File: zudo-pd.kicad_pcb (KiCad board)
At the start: 2 copper layers, 82 x 99 mm, 81 parts, among them J1 USB-C, J2 2541WR-2X08P, J3 2541WR-2X08P, J4 2541WR-2X08P, J6 1217754-1, J7 1217754-1, J8 1217754-1, J9 1217754-1, U1 CH224D, U2 LM2596S-ADJ, U3 LM2596S-ADJ, U4 LM2596S-ADJ, U6 L7812CD2T-TR, U7 L7805ABD2T-TR, U8 CJ7912_C94173

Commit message: feat: Add USBLC6-2SC6 footprint and sync schematic to PCB
- Add SOT-23-6 footprint for D4 (USBLC6-2SC6) to library
- Sync all schematic changes to PCB layout

Co-Authored-By: Claude <noreply@anthropic.com>
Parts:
- removed ?: , 
- removed J3, J4: 2541WR-2X08P, zudo-pd:HDR-TH_16P-P2.54-H-M-R2-C8-S2.54
- removed REF** (x6): MountingHole_3.2mm_M3, MountingHole:MountingHole_3.2mm_M3
- added C34: 1uF 16V, zudo-pd:C0603, F.Cu at (81.8, -22.6)
- added C35: 100nF 50V, zudo-pd:C0805, F.Cu at (83.7, -30.8)
- added D4: USBLC6-2SC6, zudo-pd:SOT-23-6_L2.9-W1.6-P0.95-LS2.8-BL, F.Cu at (65.8, -22.2)
- added Q1: -30V -4A, zudo-pd:SOT-23_L2.9-W1.3-P1.90-LS2.4-BR, F.Cu at (64.5, -8.35)
- C30: value 1uF -> 1uF 16V
- R11: value 56k -> 100k
- R12: value 5.1k -> 56k
- R13: value 5.1k -> 470
- U1: value CH224D -> STUSB4500QTR; footprint zudo-pd:QFN-20_L3.0-W3.0-P0.40-BL-EP1.7 -> zudo-pd:QFN-24_L4.0-W4.0-P0.50-BL-EP2.8
- moved R12 59.7 mm to (85.7, -22.9)
- moved R13 57.3 mm to (85.7, -20.4), turned to 0 degrees
- moved C30 55.4 mm to (81.8, -25.3), turned to 0 degrees
- moved R11 50.5 mm to (85.7, -25.4)
- moved U1 8.08 mm to (43.5, 6.00), turned to 90 degrees
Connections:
- C1 pad 2: +15V -> +13.5V gen -> VBUS_IN
- C2 pad 2: +15V -> +13.5V gen -> VBUS_IN
- C30 pad 1: Net-(U1-VDD) -> Net-(U1-VREG_2V7)
- J1 pad A9: +15V -> +13.5V gen -> VBUS_IN
- J1 pad B9: +15V -> +13.5V gen -> VBUS_IN
- J2 pad 1: -12V rail -> GATE rail
- J2 pad 10: +12V rail -> GND
- J2 pad 11: +5V rail -> GND
- J2 pad 12: +5V rail -> GND
- J2 pad 13: CV rail -> GND
- J2 pad 14: CV rail -> GND
- J2 pad 15: GATE rail -> -12V rail
- J2 pad 16: GATE rail -> -12V rail
- J2 pad 2: -12V rail -> GATE rail
- J2 pad 3: GND -> CV rail
- J2 pad 4: GND -> CV rail
- J2 pad 5: GND -> +5V rail
- J2 pad 6: GND -> +5V rail
- J2 pad 7: GND -> +12V rail
- J2 pad 8: GND -> +12V rail
- J2 pad 9: +12V rail -> GND
- R11 pad 1: Net-(U1-CFG1) -> Net-(Q1-G)
- R11 pad 2: GND -> VBUS_IN
- R12 pad 1: GND -> Net-(U1-VBUS_EN_SNK)
- R12 pad 2: Net-(J1-CC2) -> Net-(Q1-G)
- R13 pad 1: GND -> +15V -> +13.5V gen
- R13 pad 2: Net-(J1-CC1) -> Net-(U1-DISCH)
- U1 pad 1: Net-(U1-CFG1) -> Net-(U1-CC1)
- U1 pad 10: Net-(J1-CC1) -> GND
- U1 pad 11: Net-(J1-CC2) -> unconnected-(U1-ATTACH-Pad11)
- U1 pad 12: unconnected-(U1-CFG3-Pad12) -> GND
- U1 pad 13: unconnected-(U1-CFG2-Pad13) -> GND
- U1 pad 14: GND -> unconnected-(U1-POWER_OK3-Pad14)
- U1 pad 15: GND -> unconnected-(U1-GPIO-Pad15)
- U1 pad 16: unconnected-(U1-NC-Pad16) -> Net-(U1-VBUS_EN_SNK)
- U1 pad 19: Net-(U1-CFG1) -> unconnected-(U1-ALERT-Pad19)
- U1 pad 2: +15V -> +13.5V gen -> Net-(U1-CC1)
- U1 pad 21: GND -> Net-(U1-VREG_1V2)
- U1 pad 4: unconnected-(U1-NC-Pad4) -> Net-(U1-CC2)
- U1 pad 5: unconnected-(U1-GATE-Pad5) -> Net-(U1-CC2)
- U1 pad 7: Net-(U1-VDD) -> unconnected-(U1-SCL-Pad7)
- U1 pad 8: Net-(U1-DM) -> unconnected-(U1-SDA-Pad8)
- U1 pad 9: Net-(U1-DM) -> Net-(U1-DISCH)
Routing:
- net +15V -> +13.5V gen: track 156.3 -> 0.00 mm, vias 5 -> 0
- net VBUS_IN: track 0.00 -> 153.5 mm, vias 0 -> 5
- net CV rail: track 132.2 -> 5.12 mm, vias 4 -> 0
- net GND: track 172.8 -> 284.2 mm, vias 138 -> 136
- net -12V rail: track 186.6 -> 296.0 mm
- net GATE rail: track 114.5 -> 5.09 mm
- net Net-(J1-CC2): track 26.8 -> 1.54 mm, vias 2 -> 1
- net Net-(J1-CC1): track 25.4 -> 1.56 mm, vias 2 -> 1
- net Net-(U1-CFG1): track 6.91 -> 0.00 mm, vias 2 -> 0
- net (no net): track 0.00 -> 5.69 mm, vias 0 -> 1
- net Net-(U1-VDD): track 1.43 -> 0.00 mm

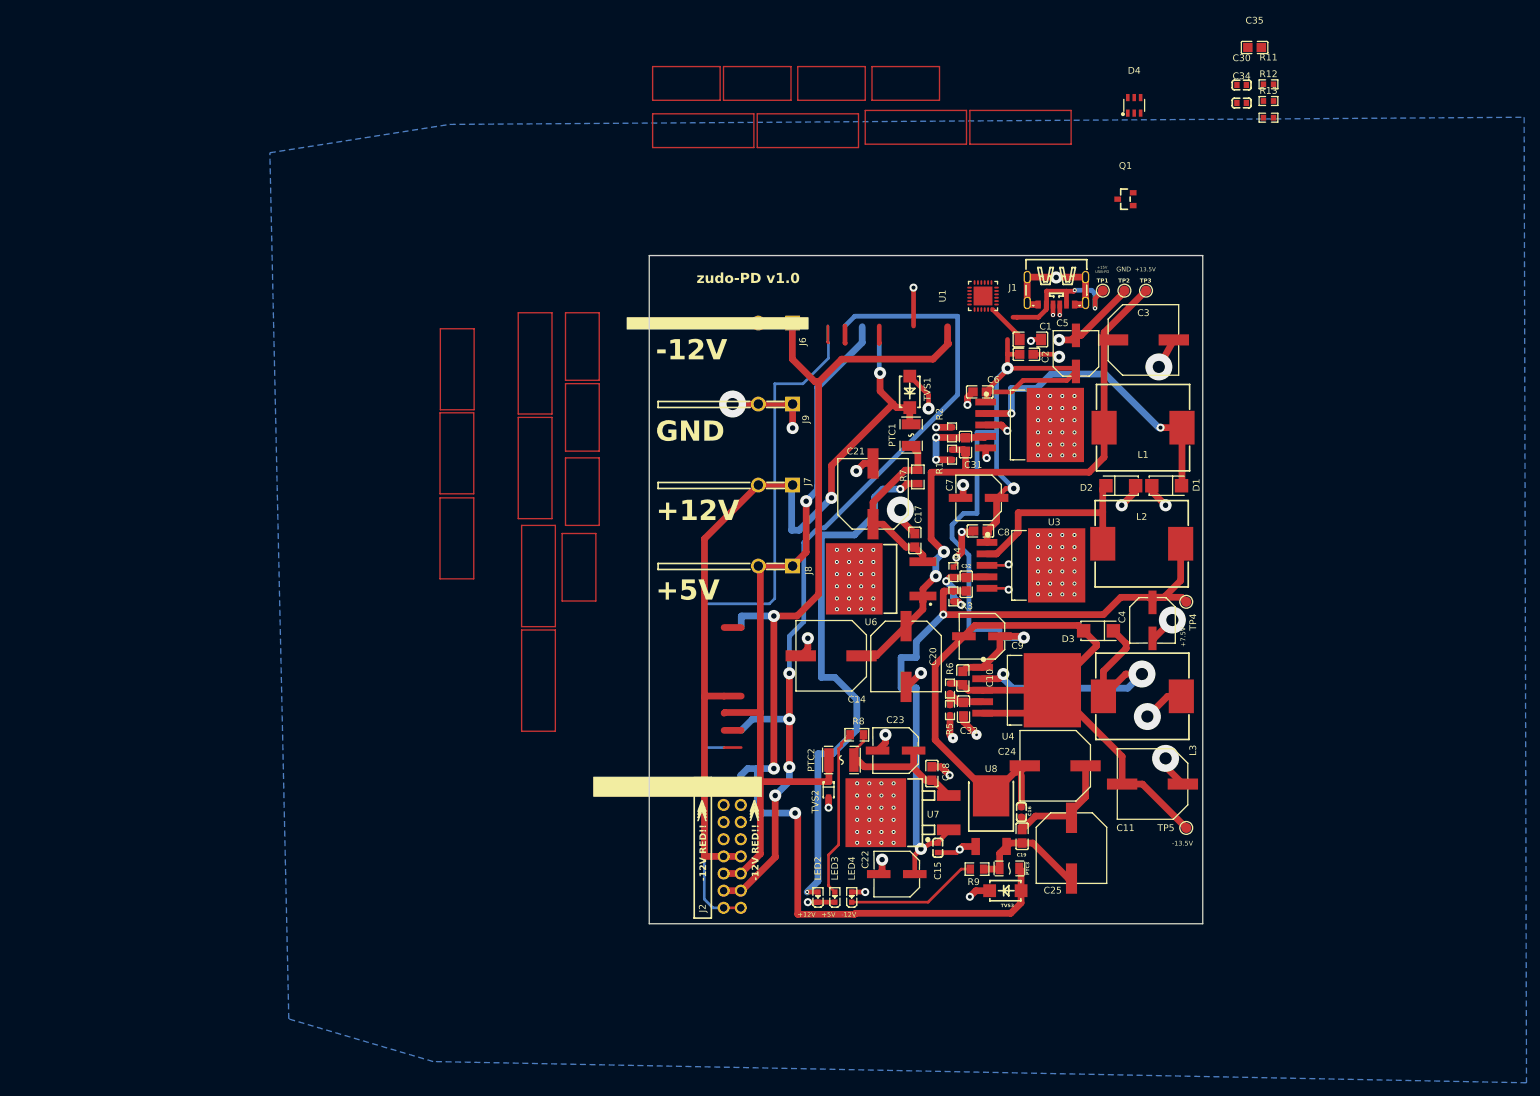
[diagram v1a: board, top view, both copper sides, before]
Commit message: feat: Update PCB layout and output schematic positioning
- Reposition components and connections in output.kicad_sch
- Update PCB layout in zudo-pd.kicad_pcb
- Add 0.25mm track width option to project settings

Co-Authored-By: Claude Sonnet 4.5 <noreply@anthropic.com>
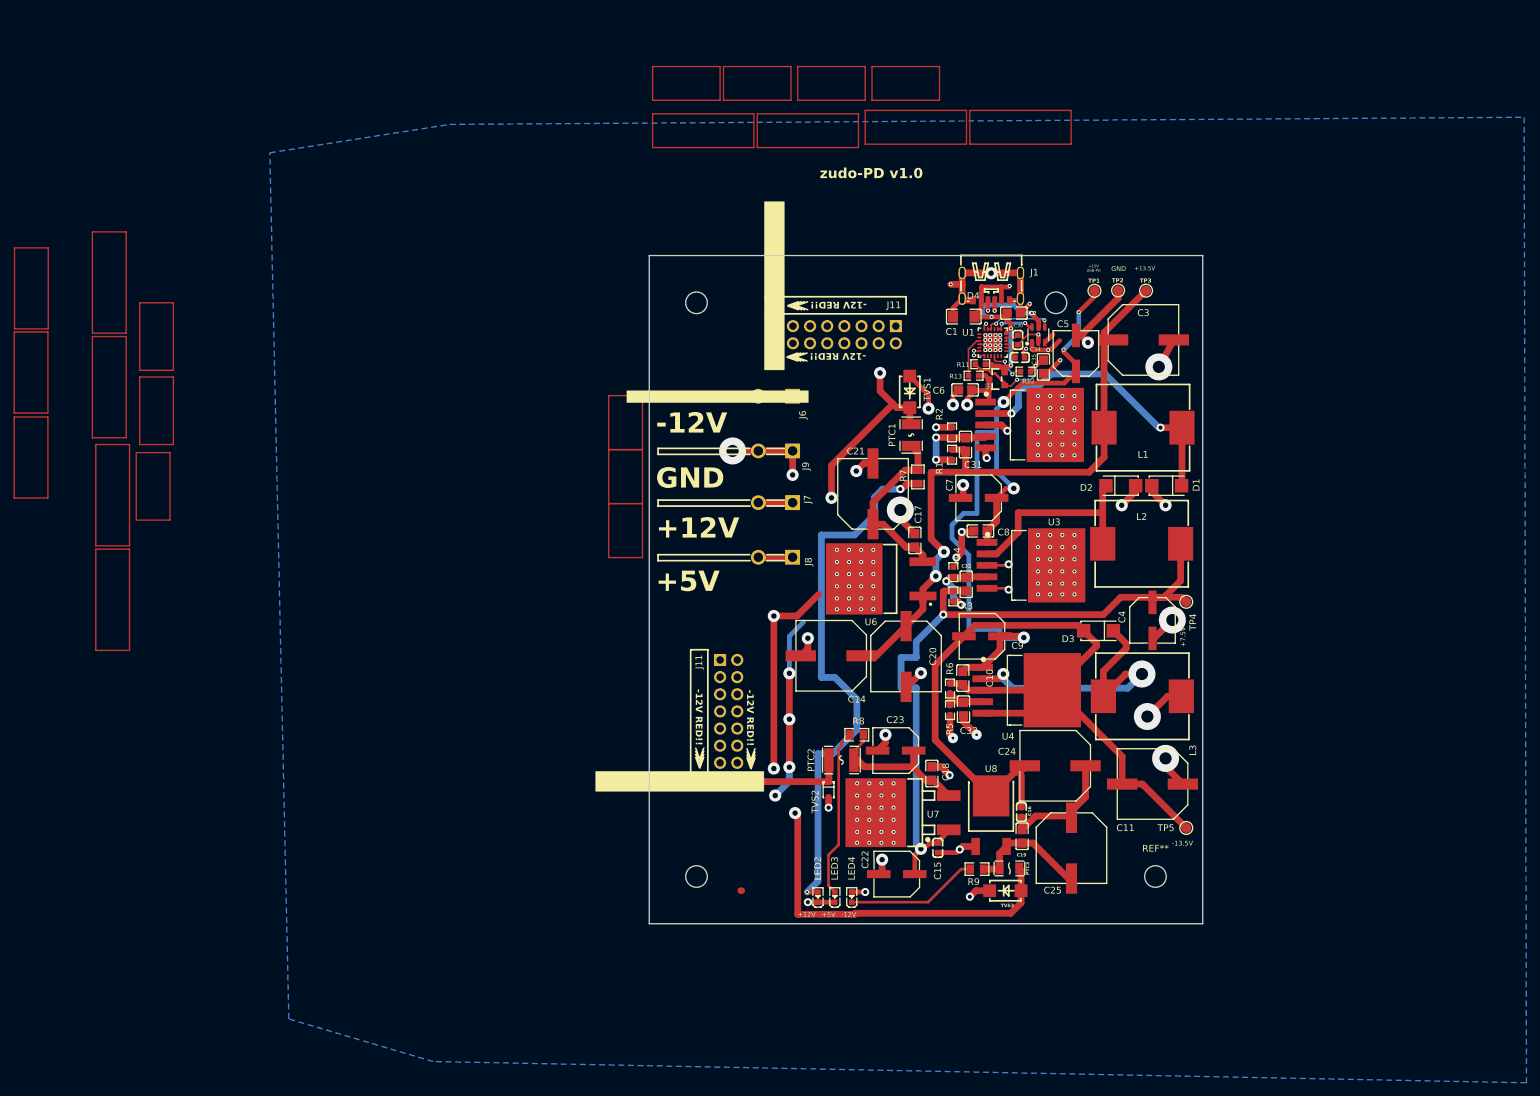
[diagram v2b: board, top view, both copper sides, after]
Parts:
- added J11: 2541WR-2X08P, zudo-pd:HDR-TH_16P-P2.54-H-M-R2-C8-S2.54, F.Cu at (21.6, 11.7)
- added REF**: MountingHole_3.2mm_M3, MountingHole:MountingHole_3.2mm_M3, F.Cu at (1.00, 92.0)
- added REF**: MountingHole_3.2mm_M3, MountingHole:MountingHole_3.2mm_M3, F.Cu at (54.2, 7.00)
- added REF**: MountingHole_3.2mm_M3, MountingHole:MountingHole_3.2mm_M3, F.Cu at (1.00, 7.00)
- added REF**: MountingHole_3.2mm_M3, MountingHole:MountingHole_3.2mm_M3, F.Cu at (69.0, 92.0)
- moved R11 59.5 mm to (43.0, 16.1)
- moved R13 58.1 mm to (42.0, 17.8), turned to 180 degrees
- moved C35 56.7 mm to (52.4, 16.5), turned to -90 degrees
- moved R12 53.9 mm to (49.8, 17.2)
- moved C30 50.3 mm to (48.6, 12.5), turned to -90 degrees
- moved C34 50.0 mm to (48.9, 15.1)
- moved D4 36.8 mm to (51.6, 11.8)
- moved Q1 32.8 mm to (45.5, 18.3)
- moved J11 18.9 mm to (5.77, 68.8)
- moved J6 10.9 mm to (12.7, 20.9)
- moved C1 10.4 mm to (40.6, 9.05), turned to 0 degrees
- moved J1 9.66 mm to (44.7, 4.60)
- moved U1 7.05 mm to (44.9, 12.9), turned to 180 degrees
- moved J9 6.95 mm to (12.7, 28.9)
- moved C2 6.39 mm to (48.0, 8.52)
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- renumbered J2 to J11
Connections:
- net +15V -> +13.5V gen renamed VBUS_OUT
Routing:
- net -12V rail: track 296.0 -> 59.2 mm, vias 3 -> 1
- net VBUS_OUT: track 0.00 -> 118.6 mm, vias 0 -> 6
- net VBUS_IN: track 153.5 -> 42.8 mm
- net +5V rail: track 113.0 -> 18.9 mm, vias 1 -> 0
- net +12V rail: track 124.5 -> 33.8 mm
- net GND: track 284.2 -> 201.7 mm, vias 136 -> 158
- net GATE rail: track 5.09 -> 30.6 mm, vias 0 -> 2
- net Net-(Q1-G): track 0.00 -> 15.2 mm, vias 0 -> 2
- net Net-(U1-CC2): track 0.00 -> 10.8 mm, vias 0 -> 2
- net Net-(U1-CC1): track 0.00 -> 6.59 mm, vias 0 -> 2
- net Net-(U1-DISCH): track 0.00 -> 6.03 mm
- net Net-(U1-VBUS_EN_SNK): track 0.00 -> 6.00 mm, vias 0 -> 2
- net Net-(J1-CC1): track 1.56 -> 7.37 mm, vias 1 -> 2
- net (no net): track 5.69 -> 0.00 mm, vias 1 -> 0
- net CV rail: track 5.12 -> 0.00 mm
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
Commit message: feat: Refine PCB layout with improved net naming
- Update net names for clarity (GND → GND rail, VBUS_OUT → +15V -> +13.5V gen)
- Adjust component reference label positions for J7, J9
- Continue PCB layout refinements for output connectors

Co-Authored-By: Claude Sonnet 4.5 <noreply@anthropic.com>
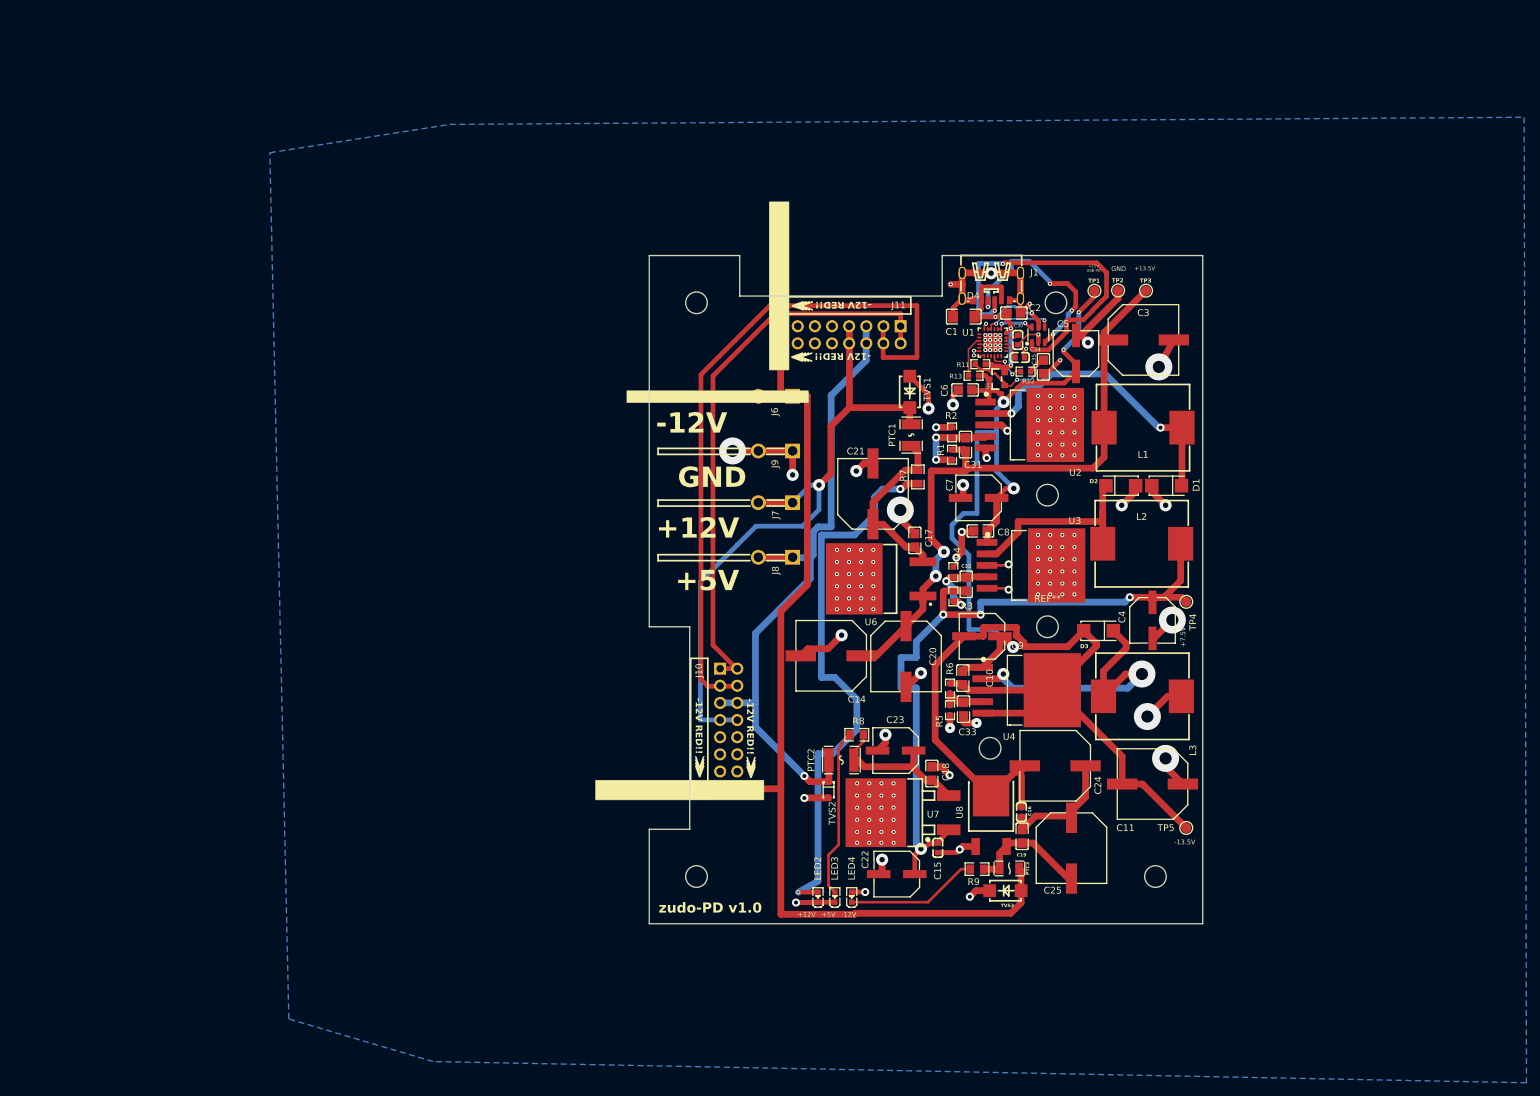
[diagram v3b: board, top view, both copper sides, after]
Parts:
- added REF**: MountingHole_3.2mm_M3, MountingHole:MountingHole_3.2mm_M3, F.Cu at (44.5, 73.0)
- added REF**: MountingHole_3.2mm_M3, MountingHole:MountingHole_3.2mm_M3, F.Cu at (53.0, 55.0)
- added REF**: MountingHole_3.2mm_M3, MountingHole:MountingHole_3.2mm_M3, F.Cu at (53.0, 35.5)
- moved J10 1.28 mm to (5.77, 70.1)
- moved J11 0.71 mm to (22.4, 11.7)
- renumbered J11 to J10
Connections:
- net VBUS_OUT renamed +15V -> +13.5V gen
- C1 pad 1: GND -> GND rail
- C11 pad 1: GND -> GND rail
- C14 pad 2: GND -> GND rail
- C15 pad 2: GND -> GND rail
- C17 pad 1: GND -> GND rail
- C18 pad 2: GND -> GND rail
- C2 pad 1: GND -> GND rail
- C20 pad 2: GND -> GND rail
- C21 pad 2: GND -> GND rail
- C22 pad 2: GND -> GND rail
- C23 pad 2: GND -> GND rail
- C3 pad 2: GND -> GND rail
- C30 pad 2: GND -> GND rail
- C33 pad 1: GND -> GND rail
- C34 pad 2: GND -> GND rail
- C35 pad 2: GND -> GND rail
- C4 pad 2: GND -> GND rail
- C5 pad 2: GND -> GND rail
- C6 pad 2: GND -> GND rail
- C7 pad 2: GND -> GND rail
- C8 pad 2: GND -> GND rail
- D1 pad 2: GND -> GND rail
- D2 pad 2: GND -> GND rail
- D4 pad 2: GND -> GND rail
- J1 pad 7: GND -> GND rail
- J1 pad A12: GND -> GND rail
- J1 pad B12: GND -> GND rail
- J10 pad 10: GND -> GND rail
- J10 pad 11: GND -> GND rail
- J10 pad 12: GND -> GND rail
- J10 pad 13: GND -> GND rail
- J10 pad 14: GND -> GND rail
- J10 pad 9: GND -> GND rail
- J11 pad 1: (no net) -> GATE rail
- J11 pad 10: (no net) -> GND rail
- J11 pad 11: (no net) -> GND rail
- J11 pad 12: (no net) -> GND rail
- J11 pad 13: (no net) -> GND rail
- J11 pad 14: (no net) -> GND rail
- J11 pad 15: (no net) -> -12V rail
- J11 pad 16: (no net) -> -12V rail
- J11 pad 2: (no net) -> GATE rail
- J11 pad 3: (no net) -> CV rail
- J11 pad 4: (no net) -> CV rail
- J11 pad 5: (no net) -> +5V rail
- J11 pad 6: (no net) -> +5V rail
- J11 pad 7: (no net) -> +12V rail
- J11 pad 8: (no net) -> +12V rail
- J11 pad 9: (no net) -> GND rail
- J9 pad 1: GND -> GND rail
- J9 pad 2: GND -> GND rail
- L3 pad 2: GND -> GND rail
- LED2 pad 1: GND -> GND rail
- LED3 pad 1: GND -> GND rail
- LED4 pad 2: GND -> GND rail
- R2 pad 1: GND -> GND rail
- R4 pad 2: GND -> GND rail
- R5 pad 2: GND -> GND rail
- TP2 pad 1: GND -> GND rail
- TVS1 pad 2: GND -> GND rail
- TVS2 pad 1: GND -> GND rail
- TVS3 pad 1: GND -> GND rail
- U1 pad 10: GND -> GND rail
- U1 pad 12: GND -> GND rail
- U1 pad 13: GND -> GND rail
- U1 pad 25: GND -> GND rail
- U1 pad 6: GND -> GND rail
- U2 pad 3: GND -> GND rail
- U2 pad 5: GND -> GND rail
- U2 pad 6: GND -> GND rail
- U3 pad 3: GND -> GND rail
- U3 pad 5: GND -> GND rail
- U3 pad 6: GND -> GND rail
- U6 pad 4: GND -> GND rail
- U7 pad 2: GND -> GND rail
- U8 pad 1: GND -> GND rail
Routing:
- net GND: track 201.7 -> 0.00 mm, vias 158 -> 0
- net GND rail: track 0.00 -> 181.2 mm, vias 0 -> 154
- net CV rail: track 0.00 -> 104.6 mm
- net -12V rail: track 59.2 -> 150.7 mm, vias 1 -> 0
- net +5V rail: track 18.9 -> 103.4 mm, vias 0 -> 1
- net +12V rail: track 33.8 -> 104.3 mm, vias 2 -> 1
- net GATE rail: track 30.6 -> 83.5 mm, vias 2 -> 0
- net Net-(J1-CC1): track 7.37 -> 50.9 mm
- net Net-(J1-CC2): track 3.12 -> 30.4 mm, vias 1 -> 4
- net VBUS_IN: track 42.8 -> 37.4 mm, vias 5 -> 4
- net /DC-DC Conversion/-13.5V OUT: track 130.5 -> 134.1 mm
- net Net-(LED2-A): track 81.0 -> 83.3 mm
- net +15V -> +13.5V gen: track 118.6 -> 117.2 mm, vias 6 -> 5
- net /DC-DC Conversion/+7.5V OUT: track 105.8 -> 106.8 mm, vias 2 -> 4
- added copper zone on B.Cu, net GND rail
- removed copper zone on B.Cu, net GND
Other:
- outline, holes or cut-outs redrawn
